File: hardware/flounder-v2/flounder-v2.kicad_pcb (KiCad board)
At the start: 2 copper layers, 100 x 100 mm, 11 parts, among them U1 Z8S180, U2 AS6C4008-55PCN, U3 SST39SF040, X1 18.432MHz

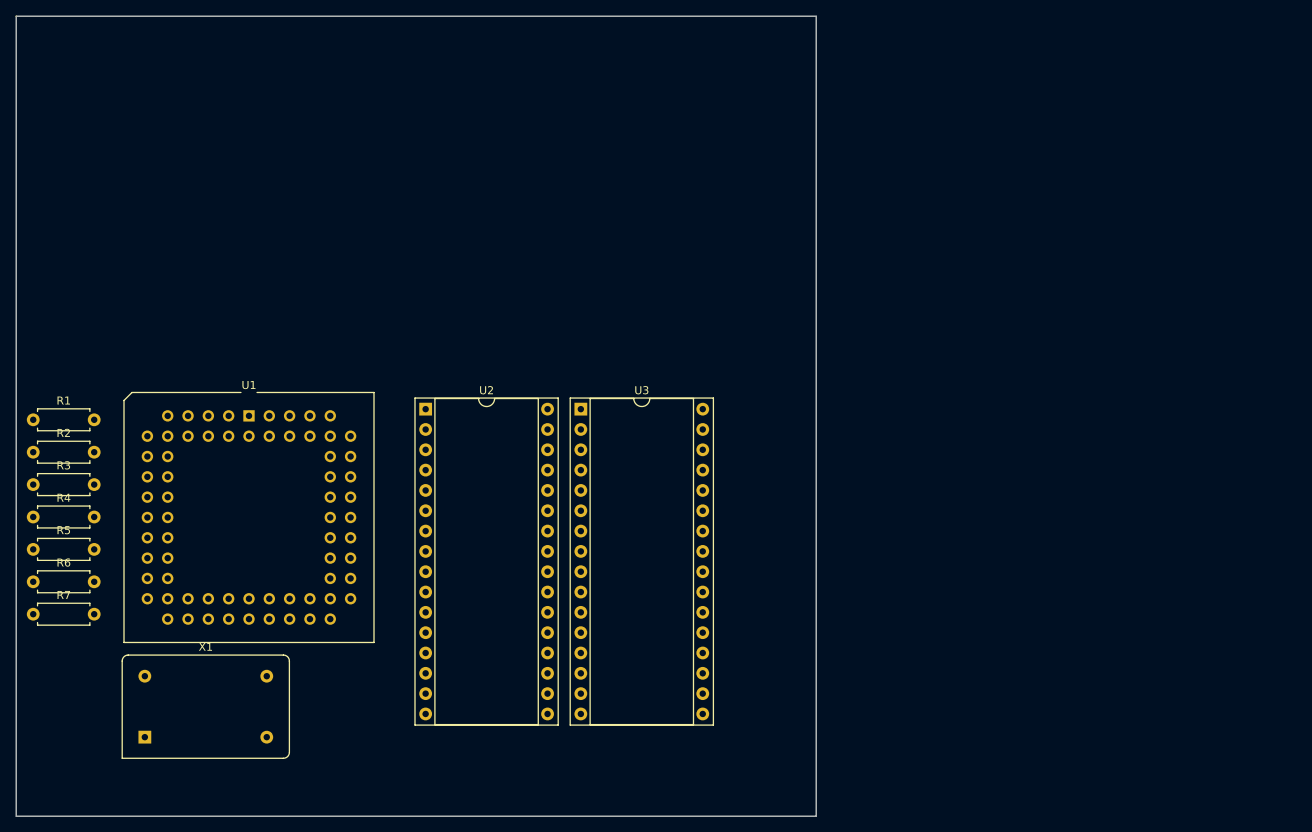
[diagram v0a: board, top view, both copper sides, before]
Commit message: Add PIO to v2
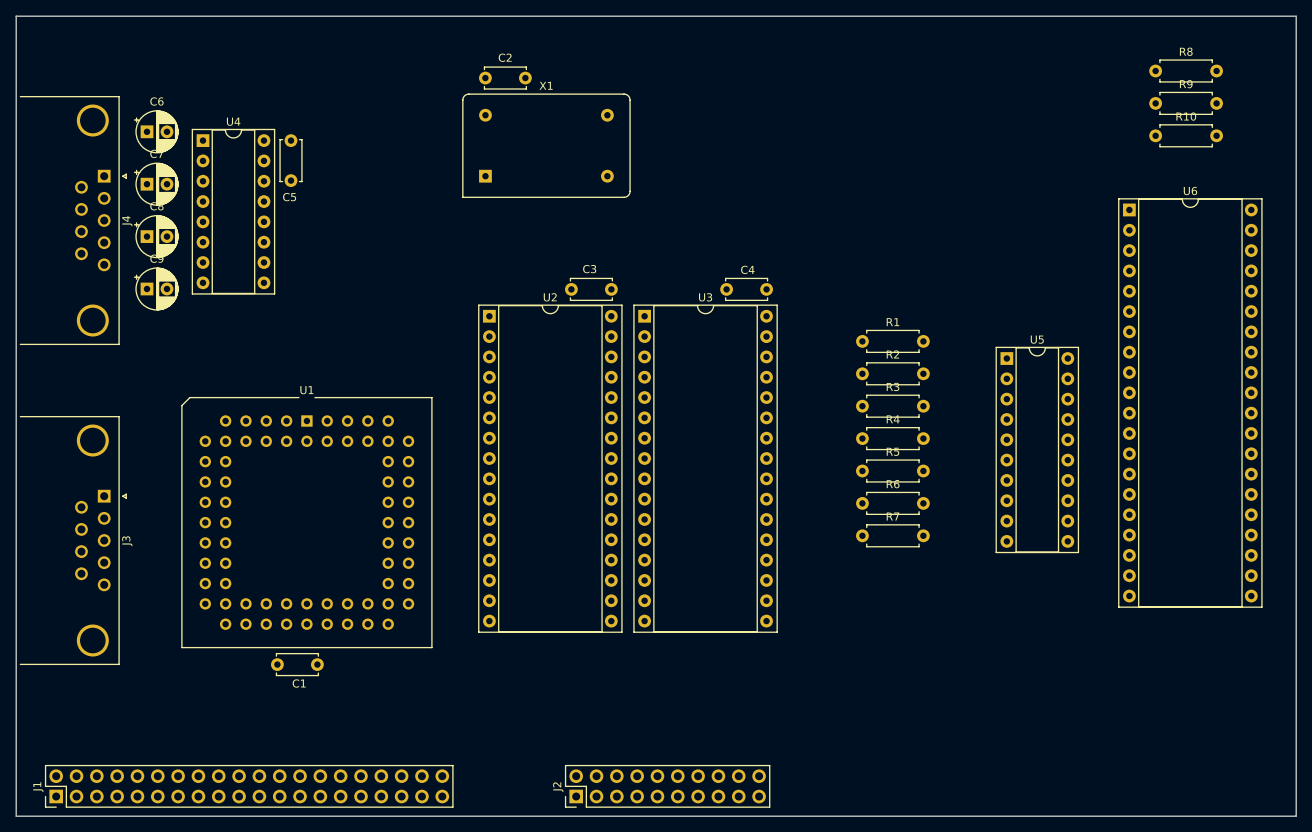
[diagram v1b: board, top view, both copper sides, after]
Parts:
- added C1: 0.1uF, Capacitor_THT:C_Disc_D5.0mm_W2.5mm_P5.00mm, F.Cu at (52.6, 101.0)
- added C2: 0.1uF, Capacitor_THT:C_Disc_D5.0mm_W2.5mm_P5.00mm, F.Cu at (78.7, 27.7)
- added C3: 0.1uF, Capacitor_THT:C_Disc_D5.0mm_W2.5mm_P5.00mm, F.Cu at (94.4, 54.1)
- added C4: 0.1uF, Capacitor_THT:C_Disc_D5.0mm_W2.5mm_P5.00mm, F.Cu at (113.8, 54.1)
- added C5: 0.1uF, Capacitor_THT:C_Disc_D5.0mm_W2.5mm_P5.00mm, F.Cu at (54.4, 35.5)
- added C6: 1uF, Capacitor_THT:CP_Radial_D5.0mm_P2.50mm, F.Cu at (36.4, 34.5)
- added C7: 1uF, Capacitor_THT:CP_Radial_D5.0mm_P2.50mm, F.Cu at (36.4, 41.0)
- added C8: 1uF, Capacitor_THT:CP_Radial_D5.0mm_P2.50mm, F.Cu at (36.4, 47.5)
- added C9: 1uF, Capacitor_THT:CP_Radial_D5.0mm_P2.50mm, F.Cu at (36.4, 54.1)
- added J1: Conn_02x20_Odd_Even, Connector_PinHeader_2.54mm:PinHeader_2x20_P2.54mm_Vertical, F.Cu at (25.0, 117.5)
- added J2: Conn_02x10_Odd_Even, Connector_PinHeader_2.54mm:PinHeader_2x10_P2.54mm_Vertical, F.Cu at (90.0, 117.5)
- added J3: DE9_Plug_MountingHoles, Connector_Dsub:DSUB-9_Male_Horizontal_P2.77x2.84mm_EdgePinOffset7.70mm_Housed_MountingHolesOffset9.12mm, F.Cu at (31.0, 80.0)
- added J4: DE9_Plug_MountingHoles, Connector_Dsub:DSUB-9_Male_Horizontal_P2.77x2.84mm_EdgePinOffset7.70mm_Housed_MountingHolesOffset9.12mm, F.Cu at (31.0, 40.0)
- added R10: 4k7, Resistor_THT:R_Axial_DIN0207_L6.3mm_D2.5mm_P7.62mm_Horizontal, F.Cu at (162.4, 35.0)
- added R8: 4k7, Resistor_THT:R_Axial_DIN0207_L6.3mm_D2.5mm_P7.62mm_Horizontal, F.Cu at (162.4, 26.9)
- added R9: 4k7, Resistor_THT:R_Axial_DIN0207_L6.3mm_D2.5mm_P7.62mm_Horizontal, F.Cu at (162.4, 30.9)
- added U4: MAX232, Package_DIP:DIP-16_W7.62mm_Socket, F.Cu at (43.4, 35.5)
- added U5: GAL16V8, Package_DIP:DIP-20_W7.62mm_Socket, F.Cu at (143.8, 62.8)
- added U6: Z84C20, Package_DIP:DIP-40_W15.24mm_Socket, F.Cu at (159.2, 44.2)
- moved R1 104.1 mm to (125.8, 60.6)
- moved R2 104.1 mm to (125.8, 64.7)
- moved R3 104.1 mm to (125.8, 68.8)
- moved R4 104.1 mm to (125.8, 72.8)
- moved R5 104.1 mm to (125.8, 76.8)
- moved R6 104.1 mm to (125.8, 80.9)
- moved R7 104.1 mm to (125.8, 85.0)
- moved X1 82.0 mm to (78.7, 40.0)
- moved U2 14.1 mm to (79.2, 57.5)
- moved U3 14.1 mm to (98.5, 57.5)
- moved U1 7.27 mm to (56.3, 70.6)
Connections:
- U1 pad 46: unconnected-(U1-/CTS0-Pad46) -> /CTS0
- U1 pad 47: unconnected-(U1-/DCD0-Pad47) -> /DCD0
- U1 pad 56: unconnected-(U1-RXS//CTS1-Pad56) -> /CTS1
- U2 pad 22: unconnected-(U2-CE#-Pad22) -> /SRAM
- U2 pad 24: unconnected-(U2-OE#-Pad24) -> GND
- U2 pad 29: unconnected-(U2-WE#-Pad29) -> /WR
- U3 pad 22: unconnected-(U3-CE-Pad22) -> /ROM
- U3 pad 24: unconnected-(U3-OE-Pad24) -> GND
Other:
- board size 100 x 100 mm -> 160 x 100 mm
